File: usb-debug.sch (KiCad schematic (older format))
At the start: 77 parts, among them IC15 TLV70018DCKT, IC16 AP22652W6-7, IC7 HD3SS3220, J11 632723300011, Q1 PMV32UP, T6 BSS138APW, T7 BSS138APW

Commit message: Change R50 to 12k4
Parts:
- removed R50: 10k2, jetson-nano-baseboard-footprints:0402, symbol jetson-nano-baseboard:R_10k2_0402
- added R50: R_12k4_0402, jetson-nano-baseboard-footprints:0402-res, symbol jetson-nano-baseboard:R_12k4_0402
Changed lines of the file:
@@
-$EndComp
-$Comp
-L jetson-nano-baseboard:R_10k2_0402 R50
-U 1 1 5E7102F6
-P 5000 9775
-F 0 "R50" V 5000 9745 60  0000 R TNN
-F 1 "10k2" V 4900 9745 60  0000 R TNN
-F 2 "jetson-nano-baseboard-footprints:0402" H 4900 9745 60  0001 C CNN
-F 3 "" H 4900 9745 60  0001 C CNN
-F 4 "CPF0402B10K2E1" H -33616 -15093 50  0001 C CNN "MPN"
-F 5 "TE" H -33616 -15093 50  0001 C CNN "Manufacturer"
-	1    5000 9775
-	0    -1   -1   0
 $EndComp
 $Comp
@@
 	1    0    0    -1
 $EndComp
+$Comp
+L jetson-nano-baseboard:R_12k4_0402 R50
+U 1 1 61D47A2E
+P 5000 9775
+F 0 "R50" V 5045 9705 60  0000 R CNN
+F 1 "R_12k4_0402" H 5000 9625 60  0001 C CNN
+F 2 "jetson-nano-baseboard-footprints:0402-res" H 5200 9975 60  0001 L CNN
+F 3 "" H 5000 9775 50  0001 C CNN
+F 4 "PANASONIC_ELECTRONIC_COMPONENTS" H 5200 10175 60  0001 L CNN "Manufacturer"
+F 5 "ERJ2RKF1242X" H 5200 10075 60  0001 L CNN "MPN"
+F 6 "12k4" V 4947 9705 50  0000 R CNN "Val"
+	1    5000 9775
+	0    -1   -1   0
+$EndComp
 $EndSCHEMATC

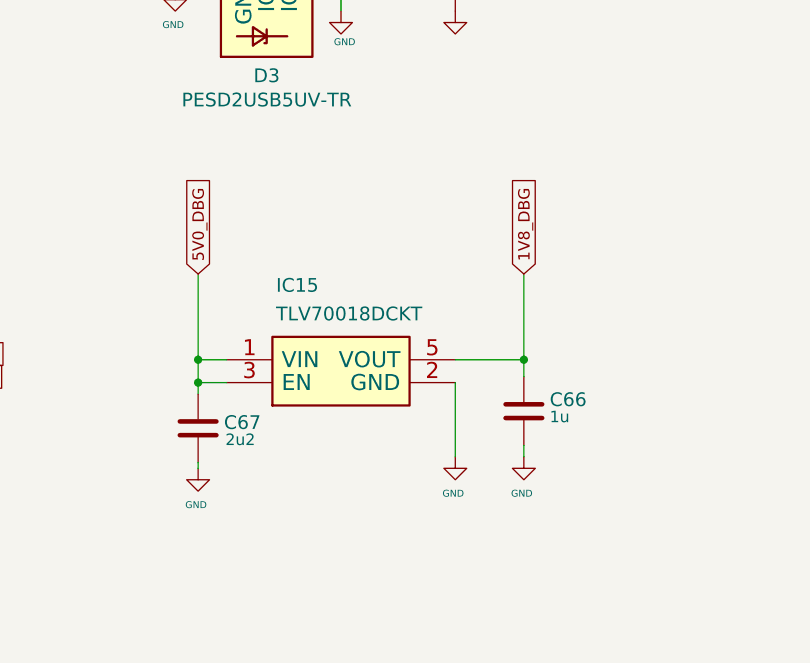
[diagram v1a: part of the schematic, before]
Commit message: Change IC15 to TPS7A0518, loclib
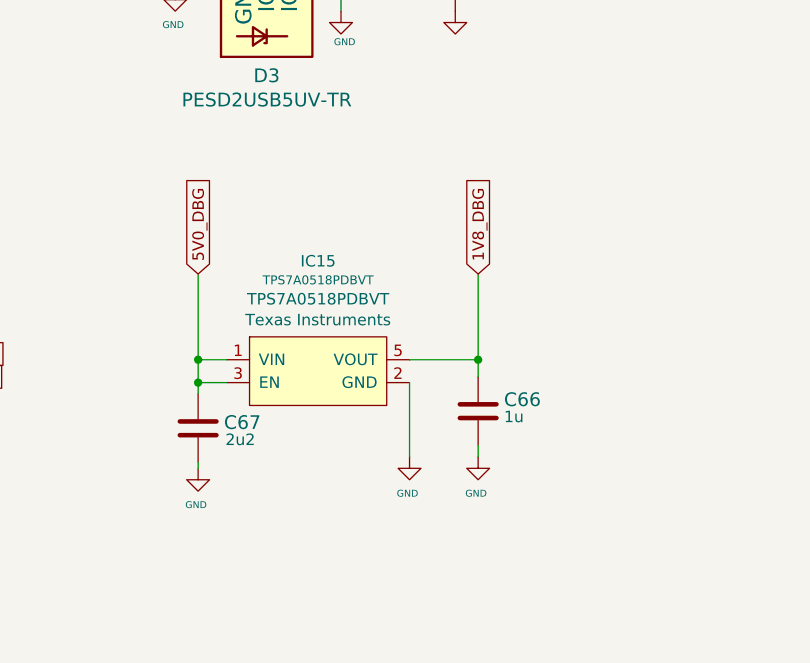
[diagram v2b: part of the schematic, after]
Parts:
- removed IC15: TLV70018DCKT, jetson-nano-baseboard-footprints:SC70-5, symbol jetson-nano-baseboard:TLV700
- added IC15: TPS7A0518PDBVT, jetson-nano-baseboard-footprints:SOT-23-5, symbol jetson-nano-baseboard:TPS7A0518PDBVT
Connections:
- net 1V8_DBG: now also IC15.5 (VOUT)
- net 5V0_DBG: now also IC15.1 (VIN), IC15.3 (EN)
- net GND: now also IC15.2 (GND)
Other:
- moved on the sheet: C66
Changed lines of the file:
@@
 Text GLabel 12975 8675 1    50   Input ~ 0
 5V0_DBG
-Text GLabel 14400 8675 1    50   Input ~ 0
+Text GLabel 14200 8675 1    50   Input ~ 0
 1V8_DBG
 Text GLabel 13375 6325 1    50   Input ~ 0
@@
 L jetson-nano-baseboard:GND #GND_0110
 U 1 1 5E710343
-P 14400 9475
-F 0 "#GND_0110" H 14400 9475 20  0001 C CNN
-F 1 "GND" H 14391 9315 30  0000 C CNN
-F 2 "" H 14400 9475 70  0001 C CNN
-F 3 "" H 14400 9475 70  0001 C CNN
-	1    14400 9475
+P 14200 9475
+F 0 "#GND_0110" H 14200 9475 20  0001 C CNN
+F 1 "GND" H 14191 9315 30  0000 C CNN
+F 2 "" H 14200 9475 70  0001 C CNN
+F 3 "" H 14200 9475 70  0001 C CNN
+	1    14200 9475
 	1    0    0    -1
 $EndComp
@@
 L jetson-nano-baseboard:GND #GND_0111
 U 1 1 5E710342
-P 14100 9475
-F 0 "#GND_0111" H 14100 9475 20  0001 C CNN
-F 1 "GND" H 14091 9315 30  0000 C CNN
-F 2 "" H 14100 9475 70  0001 C CNN
-F 3 "" H 14100 9475 70  0001 C CNN
-	1    14100 9475
+P 13900 9475
+F 0 "#GND_0111" H 13900 9475 20  0001 C CNN
+F 1 "GND" H 13891 9315 30  0000 C CNN
+F 2 "" H 13900 9475 70  0001 C CNN
+F 3 "" H 13900 9475 70  0001 C CNN
+	1    13900 9475
 	1    0    0    -1
 $EndComp
@@
 	1    6500 2800
 	0    1    1    0
-$EndComp
-$Comp
-L jetson-nano-baseboard:TLV700 IC15
-U 1 1 5E71031B
-P 13600 9150
-F 0 "IC15" H 13316 9540 60  0000 L BNN
-F 1 "TLV70018DCKT" H 13316 9415 60  0000 L BNN
-F 2 "jetson-nano-baseboard-footprints:SC70-5" H 13300 9350 60  0001 C CNN
-F 3 "" H 13300 9350 60  0001 C CNN
-F 4 "Texas Instrumets" V 1200 7057 60  0001 C CNN "Manufacturer"
-F 5 "TLV70018DCKT" H -24560 -20462 50  0001 C CNN "MPN"
-	1    13600 9150
-	1    0    0    -1
 $EndComp
 $Comp
@@
 NoConn ~ 10600 10325
 Wire Wire Line
-	14100 9150 14100 9475
-Wire Wire Line
-	14100 9050 14400 9050
-Wire Wire Line
-	14400 8675 14400 9050
+	13900 9150 13900 9475
+Wire Wire Line
+	13900 9050 14200 9050
+Wire Wire Line
+	14200 8675 14200 9050
 Wire Wire Line
 	13100 9150 12975 9150
@@
 L jetson-nano-baseboard:C_1u_0402 C66
 U 1 1 6273C14B
-P 14400 9275
-F 0 "C66" H 14125 9225 60  0000 L CNN
-F 1 "C_1u_0402" H 14400 9125 60  0001 C CNN
-F 2 "jetson-nano-baseboard-footprints:0402-cap" H 14600 9475 60  0001 L CNN
-F 3 "" H 14400 9275 50  0001 C CNN
-F 4 "TDK" H 14600 9675 60  0001 L CNN "Manufacturer"
-F 5 "C1005X6S1A105K050BC" H 14600 9575 60  0001 L CNN "MPN"
-F 6 "1u" H 14200 9300 50  0000 L CNN "Val"
-	1    14400 9275
+P 14200 9275
+F 0 "C66" H 13925 9225 60  0000 L CNN
+F 1 "C_1u_0402" H 14200 9125 60  0001 C CNN
+F 2 "jetson-nano-baseboard-footprints:0402-cap" H 14400 9475 60  0001 L CNN
+F 3 "" H 14200 9275 50  0001 C CNN
+F 4 "TDK" H 14400 9675 60  0001 L CNN "Manufacturer"
+F 5 "C1005X6S1A105K050BC" H 14400 9575 60  0001 L CNN "MPN"
+F 6 "1u" H 14000 9300 50  0000 L CNN "Val"
+	1    14200 9275
 	-1   0    0    1
 $EndComp
@@
 Connection ~ 12975 9150
 Wire Wire Line
-	14400 9425 14400 9475
-Wire Wire Line
-	14400 9125 14400 9050
-Connection ~ 14400 9050
+	14200 9425 14200 9475
+Wire Wire Line
+	14200 9125 14200 9050
+Connection ~ 14200 9050
 $Comp
 L jetson-nano-baseboard:R_22R_0402 R20
@@
 	0    -1   -1   0
 $EndComp
+$Comp
+L jetson-nano-baseboard:TPS7A0518PDBVT IC15
+U 1 1 61DDFCD3
+P 13500 9100
+F 0 "IC15" H 13500 9581 50  0000 C CNN
+F 1 "TPS7A0518PDBVT" H 13500 9498 39  0000 C CNN
+F 2 "jetson-nano-baseboard-footprints:SOT-23-5" H 13500 8850 50  0001 C CNN
+F 3 "" H 13500 9100 50  0001 C CNN
+F 4 "TPS7A0518PDBVT" H 13500 9415 50  0000 C CNN "MPN"
+F 5 "Texas Instruments" H 13500 9324 50  0000 C CNN "Manufacturer"
+	1    13500 9100
+	1    0    0    -1
+$EndComp
 $EndSCHEMATC

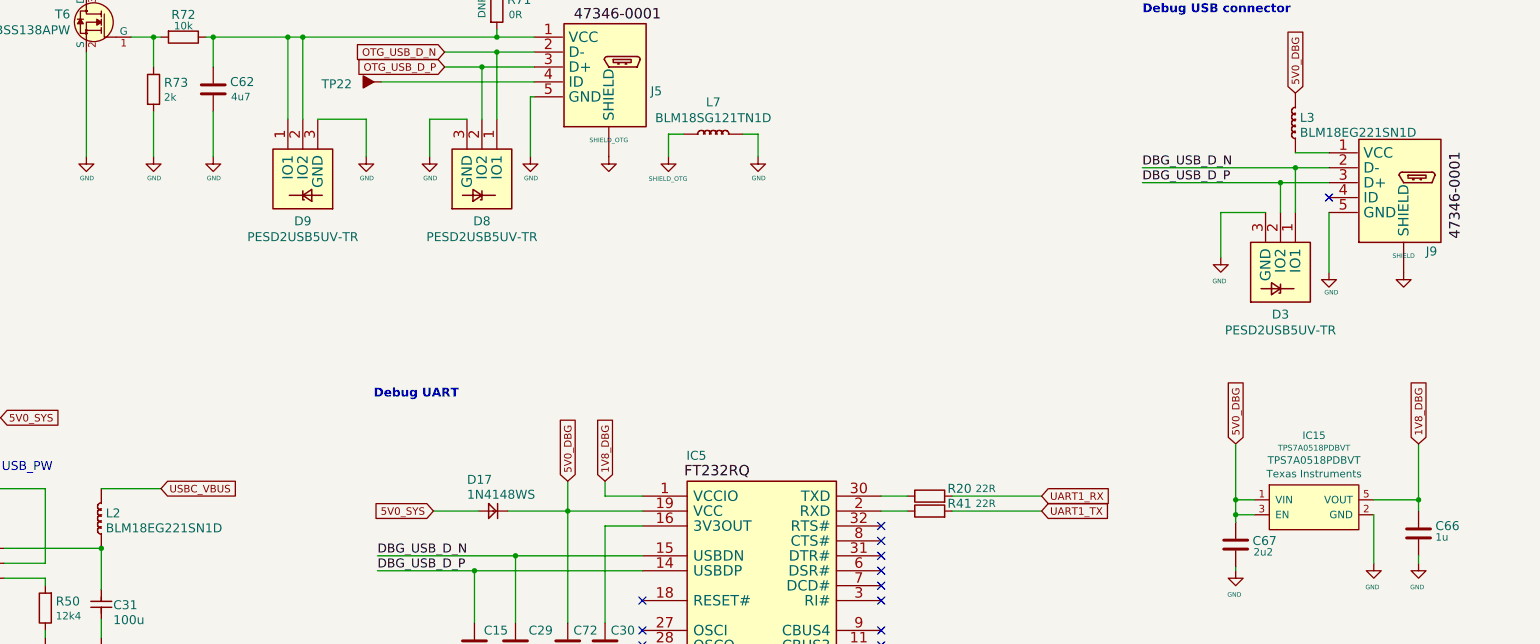
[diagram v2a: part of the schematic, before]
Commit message: Change BLM18EG221SN1D to BLM18SG121TN1D on schematic and PCB
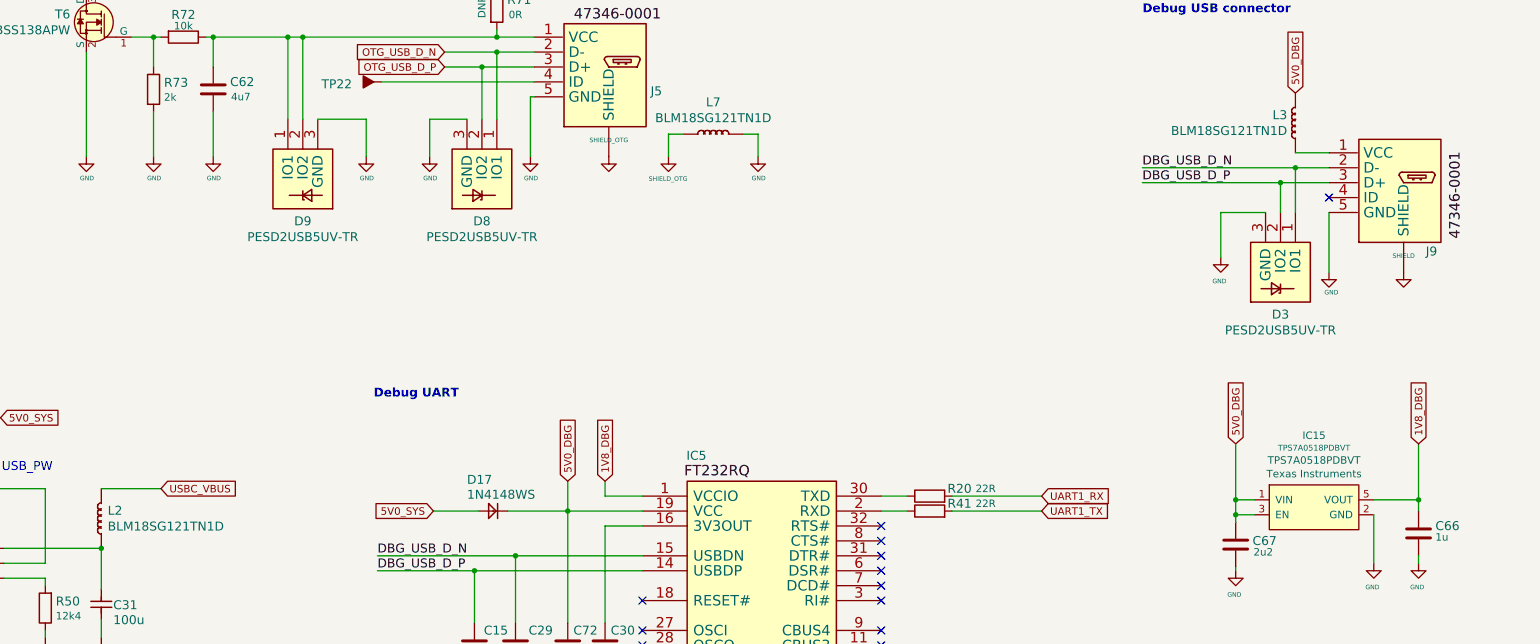
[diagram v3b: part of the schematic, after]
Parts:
- removed L2, L3: BLM18EG221SN1D, jetson-nano-baseboard-footprints:0603, symbol jetson-nano-baseboard:BLM18EG221SN1D
- added L2, L3: BLM18SG121TN1D, jetson-nano-baseboard-footprints:0603, symbol jetson-nano-baseboard:BLM18SG121TN1D
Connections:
- net 5V0_DBG: now also L3.2 (P)
- net USBC_VBUS: now also L2.2 (P)
- net at J9.1 (VCC): now also L3.1 (P)
- net at C31.2, IC16.6 (OUT): now also L2.1 (P)
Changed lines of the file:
@@
-$EndComp
-$Comp
-L jetson-nano-baseboard:BLM18EG221SN1D L2
-U 1 1 5E71031A
-P 5375 9175
-F 0 "L2" V 5375 9145 60  0000 R TNN
-F 1 "BLM18EG221SN1D" V 5275 9145 60  0000 R TNN
-F 2 "jetson-nano-baseboard-footprints:0603" H 5275 9145 60  0001 C CNN
-F 3 "" H 5275 9145 60  0001 C CNN
-F 4 "BLM18EG221SN1D" H -33741 -15093 50  0001 C CNN "MPN"
-F 5 "Murata" H -33741 -15093 50  0001 C CNN "Manufacturer"
-	1    5375 9175
-	0    -1   -1   0
 $EndComp
 $Comp
@@
 	0    1    1    0
 $EndComp
-$Comp
-L jetson-nano-baseboard:BLM18EG221SN1D L3
-U 1 1 5E7102ED
-P 13375 6525
-F 0 "L3" V 13375 6495 60  0000 R TNN
-F 1 "BLM18EG221SN1D" V 13275 6495 60  0000 R TNN
-F 2 "jetson-nano-baseboard-footprints:0603" H 13275 6495 60  0001 C CNN
-F 3 "" H 13275 6495 60  0001 C CNN
-F 4 "BLM18EG221SN1D" H -24985 -20787 50  0001 C CNN "MPN"
-F 5 "Murata" H -24985 -20787 50  0001 C CNN "Manufacturer"
-	1    13375 6525
-	0    -1   -1   0
-$EndComp
 Text GLabel 1675 5250 1    50   Input ~ 0
 5V0_SYS
@@
 Wire Wire Line
 	5375 9375 5375 9650
-Connection ~ 5375 9375
 Wire Wire Line
 	5375 8975 5775 8975
@@
 	1    0    0    -1
 $EndComp
+$Comp
+L jetson-nano-baseboard:BLM18SG121TN1D L?
+U 1 1 61FB7FE7
+P 13375 6525
+AR Path="/6096D016/61FB7FE7" Ref="L?"  Part="1"
+AR Path="/608DF3E5/61FB7FE7" Ref="L3"  Part="1"
+F 0 "L3" V 13428 6580 60  0000 L CNN
+F 1 "BLM18SG121TN1D" V 13322 6580 60  0000 L CNN
+F 2 "jetson-nano-baseboard-footprints:0603" H 13275 6125 60  0001 C CNN
+F 3 "" H 13275 6125 60  0001 C CNN
+F 4 "Murata" V 675 3032 60  0001 C CNN "Manufacturer"
+F 5 "BLM18SG121TN1D" H -15823 -14678 50  0001 C CNN "MPN"
+	1    13375 6525
+	0    -1   -1   0
+$EndComp
+$Comp
+L jetson-nano-baseboard:BLM18SG121TN1D L?
+U 1 1 61F83FCF
+P 5375 9175
+AR Path="/6096D016/61F83FCF" Ref="L?"  Part="1"
+AR Path="/608DF3E5/61F83FCF" Ref="L2"  Part="1"
+F 0 "L2" V 5428 9132 60  0000 R CNN
+F 1 "BLM18SG121TN1D" V 5322 9132 60  0000 R CNN
+F 2 "jetson-nano-baseboard-footprints:0603" H 5275 8775 60  0001 C CNN
+F 3 "" H 5275 8775 60  0001 C CNN
+F 4 "Murata" V -7325 5682 60  0001 C CNN "Manufacturer"
+F 5 "BLM18SG121TN1D" H -23823 -12028 50  0001 C CNN "MPN"
+	1    5375 9175
+	0    -1   -1   0
+$EndComp
+Connection ~ 5375 9375
 $EndSCHEMATC
